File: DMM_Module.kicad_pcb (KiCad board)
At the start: 4 copper layers, 60 x 96 mm, 110 parts, among them J1 M20-7810245, J2 M20-7810245, J3 M20-7812045, J4 M20-7812045, J5 M20-7810245, J6 M20-7810245, K1 G6K-2F-Y-TR, K2 G6K-2F-Y-TR, K3 G6K-2F-Y-TR, K4 G6K-2F-Y-TR, Q1 DMN2056U, Q2 DMN2056U, Q3 DMN2056U, Q4 DMN2056U, U1 HY3131, U2 TPS7A2401DBVR, U3 PI4IOE5V9536UEX, U4 ADUM5411BRSZ, U5 NCP164CSN330T1G, X1 4.9152MHz

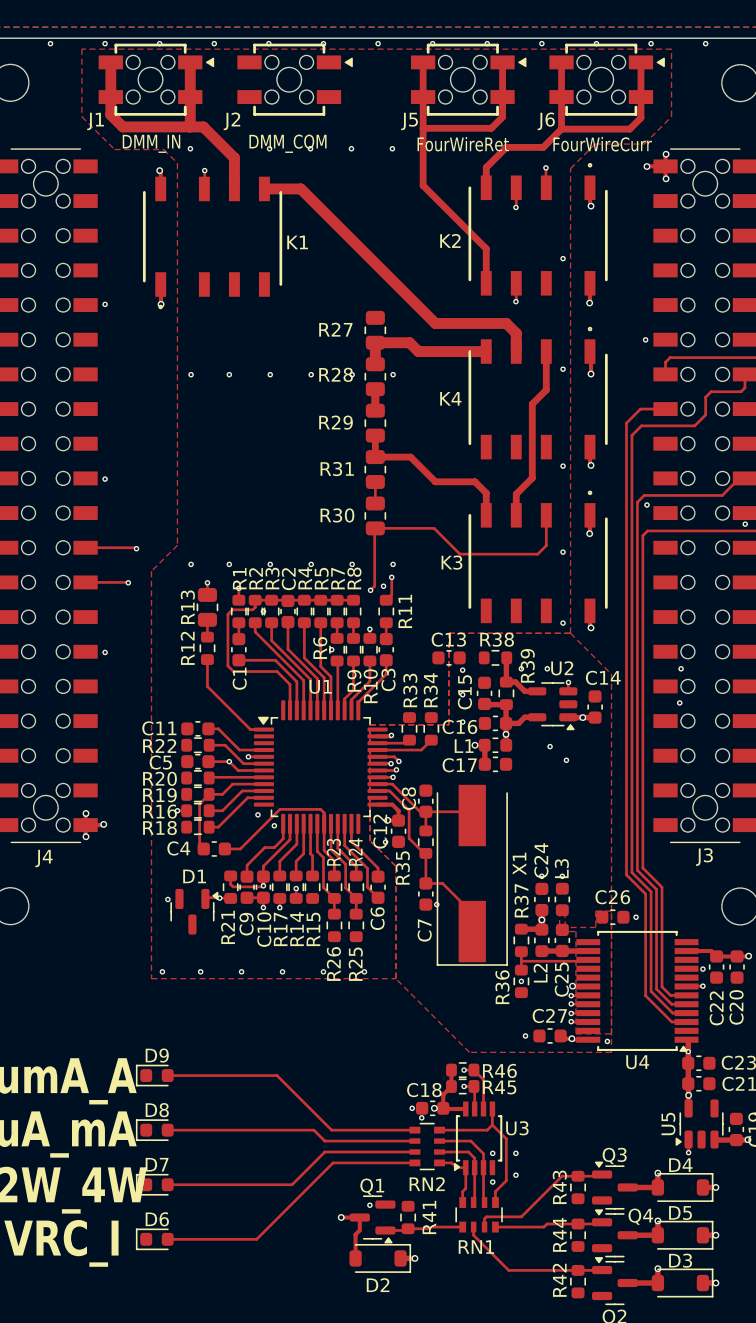
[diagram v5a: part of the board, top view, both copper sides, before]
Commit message: Schematics updated with current protection and EEPROM
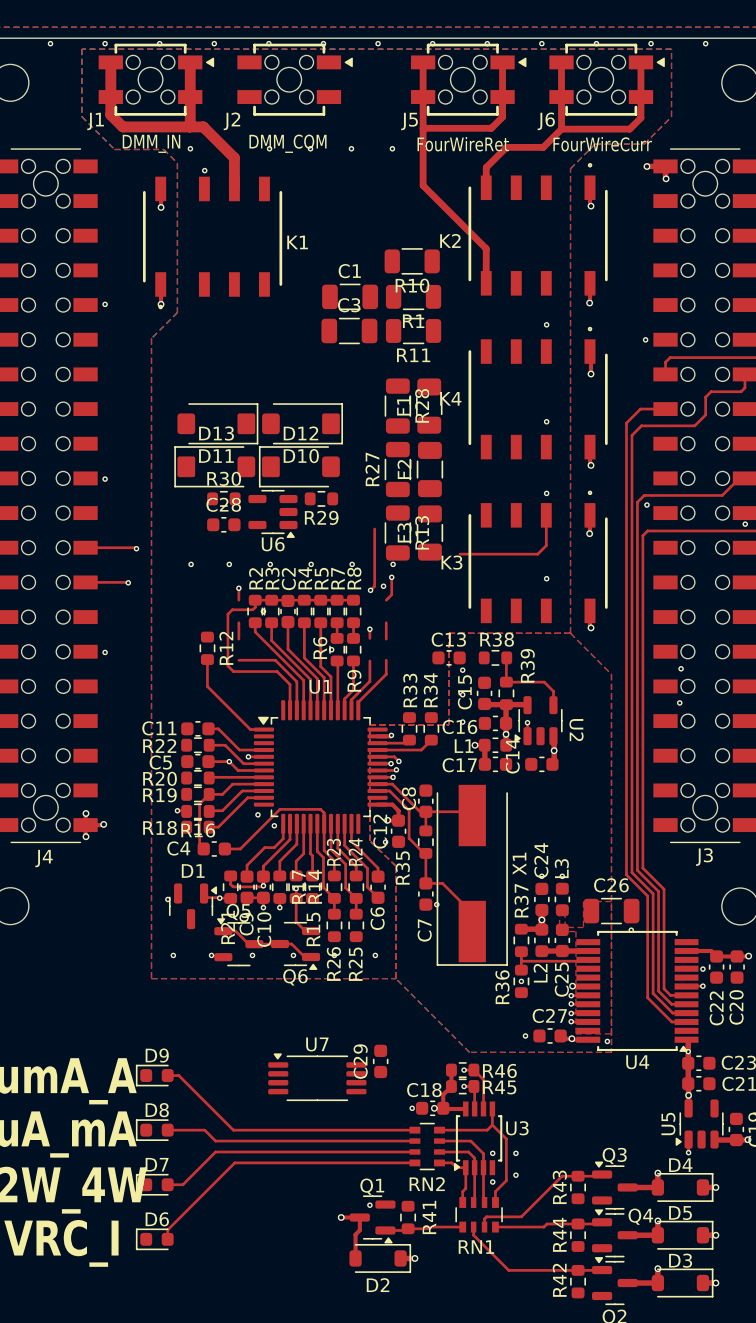
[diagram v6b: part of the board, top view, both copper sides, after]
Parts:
- removed R31: 75, Resistor_SMD:R_0805_2012Metric
- added C28: 100n, Capacitor_SMD:C_0603_1608Metric, F.Cu at (156.2, 71.2)
- added C29: 100n, Capacitor_SMD:C_0603_1608Metric, F.Cu at (167.7, 110.6)
- added D10: VS-3EJH01-M3, sesa_device:SlimSMPA, F.Cu at (161.8, 63.8)
- added D11: VS-3EJH01-M3, sesa_device:SlimSMPA, F.Cu at (155.6, 63.8)
- added D12: VS-3EJH01-M3, sesa_device:SlimSMPA, F.Cu at (161.8, 67.0)
- added D13: VS-3EJH01-M3, sesa_device:SlimSMPA, F.Cu at (155.6, 67.0)
- added F1: 50mA, Fuse:Fuse_1206_3216Metric, F.Cu at (171.2, 62.5)
- added F2: 500mA, Fuse:Fuse_1206_3216Metric, F.Cu at (171.3, 67.2)
- added F3: 2A, Fuse:Fuse_1206_3216Metric, F.Cu at (171.3, 71.8)
- added Q5: MMBT3904, Package_TO_SOT_SMD:SOT-23-3, F.Cu at (157.3, 102.0)
- added Q6: MMBT3904, Package_TO_SOT_SMD:SOT-23-3, F.Cu at (161.4, 102.0)
- added U6: TLV9061, Package_TO_SOT_SMD:SOT-23-5, F.Cu at (159.8, 70.3)
- added U7: AT24C08C, Package_SO:TSSOP-8_4.4x3mm_P0.65mm, F.Cu at (163.0, 111.8)
- C1, C3: value 5p1 -> 5p6; footprint Capacitor_SMD:C_0603_1608Metric -> Capacitor_SMD:C_1206_3216Metric
- C26: footprint Capacitor_SMD:C_0603_1608Metric -> Capacitor_SMD:C_1206_3216Metric
- R1, R10, R11: footprint Resistor_SMD:R_0603_1608Metric -> Resistor_SMD:R_1206_3216Metric
- R12: value 100 -> 10k
- R13: value 1k5 -> 20m; footprint Resistor_SMD:R_0805_2012Metric -> Resistor_SMD:R_1206_3216Metric
- R27: value 10m -> 1; footprint Resistor_SMD:R_0805_2012Metric -> Resistor_SMD:R_1206_3216Metric
- R28: value 910m -> 100; footprint Resistor_SMD:R_0805_2012Metric -> Resistor_SMD:R_1206_3216Metric
- R29: value 80m -> 10k; footprint Resistor_SMD:R_0805_2012Metric -> Resistor_SMD:R_0603_1608Metric
- R30: value 24 -> 100; footprint Resistor_SMD:R_0805_2012Metric -> Resistor_SMD:R_0603_1608Metric
- moved R10 28.6 mm to (170.0, 51.9), turned to 180 degrees
- moved C1 27.1 mm to (165.4, 54.5), turned to 0 degrees
- moved R1 26.4 mm to (170.1, 54.5), turned to 180 degrees
- moved C3 23.5 mm to (165.4, 57.0), turned to 0 degrees
- moved R11 20.6 mm to (170.1, 57.0), turned to 180 degrees
- moved R13 15.0 mm to (168.9, 71.8)
- moved R30 11.2 mm to (156.2, 69.3), turned to 0 degrees
- moved R27 10.3 mm to (168.9, 67.2)
- moved R29 6.81 mm to (163.3, 69.3), turned to 180 degrees
- moved C14 5.73 mm to (179.5, 88.8), turned to 0 degrees
- moved R28 2.71 mm to (168.9, 62.5)
- moved U2 1.50 mm to (179.4, 85.6), turned to 90 degrees
- moved C26 0.46 mm to (184.6, 99.5)
- moved D1 0.41 mm to (153.8, 99.2)
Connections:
- K1 pad 2: unconnected-(K1A-NC1-Pad2) -> /DMM DAQ/VdOhmCap
- K1 pad 3: unconnected-(K1A-COM1-Pad3) -> /DMM_IN
- K1 pad 4: unconnected-(K1A-NO1-Pad4) -> /DMM DAQ/CurrentIn
- K1 pad 5: /DMM DAQ/CurrentIn -> unconnected-(K1B-NO2-Pad5)
- K1 pad 6: /DMM_IN -> unconnected-(K1B-COM2-Pad6)
- K1 pad 7: /DMM DAQ/VdOhmCap -> unconnected-(K1B-NC2-Pad7)
- K2 pad 2: /DMM DAQ/VdOhmCap -> GNDA
- K2 pad 4: /FourWireCurr -> /FourWireRet
- K2 pad 5: /FourWireRet -> /FourWireCurr
- K2 pad 7: GNDA -> /DMM DAQ/mVOhmCap
- K3 pad 2: /DMM DAQ/I_uAmp -> Net-(K3A-NC1)
- K3 pad 4: /DMM DAQ/I_mAmp -> Net-(K3A-NO1)
- K4 pad 2: Net-(K3A-COM1) -> unconnected-(K4A-NC1-Pad2)
- K4 pad 3: /DMM DAQ/CurrentIn -> /DMM DAQ/mVOhmCap
- K4 pad 4: /DMM DAQ/I_Amp -> /DMM DAQ/VdOhmCap
- K4 pad 5: unconnected-(K4B-NO2-Pad5) -> Net-(K3A-COM1)
- K4 pad 6: unconnected-(K4B-COM2-Pad6) -> /DMM DAQ/CurrentIn
- K4 pad 7: unconnected-(K4B-NC2-Pad7) -> Net-(K4B-NC2)
- R12 pad 1: Net-(R12-Pad1) -> Net-(K2B-COM2)
- R13 pad 1: Net-(K2A-COM1) -> /DMM DAQ/I_Amp
- R13 pad 2: Net-(R12-Pad1) -> GNDA
- R14 pad 2: /DMM DAQ/VdOhmCap -> /DMM DAQ/mVOhmCap
- R16 pad 2: Net-(K2B-COM2) -> Net-(K2A-COM1)
- R27 pad 2: GNDA -> /DMM DAQ/I_mAmp
- R28 pad 1: /DMM DAQ/I_Amp -> /DMM DAQ/I_uAmp
- R28 pad 2: Net-(R28-Pad2) -> /DMM DAQ/I_mAmp
- R29 pad 1: /DMM DAQ/I_mAmp -> /DMM DAQ/I_uAmp
- R29 pad 2: Net-(R28-Pad2) -> Net-(U6-IN+)
- R30 pad 1: /DMM DAQ/I_uAmp -> Net-(D10-A)
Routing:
- net /DMM DAQ/VdOhmCap: track 104.5 -> 0.00 mm, vias 6 -> 0
- net /DMM DAQ/mVOhmCap: track 0.00 -> 58.2 mm, vias 0 -> 4
- net Net-(K2B-COM2): track 51.2 -> 0.00 mm, vias 2 -> 0
- net Net-(K2A-COM1): track 40.8 -> 0.68 mm, vias 2 -> 1
- net /DMM DAQ/CurrentIn: track 24.2 -> 0.00 mm
- net /DMM DAQ/I_uAmp: track 47.1 -> 31.3 mm
- net Net-(K3A-COM1): track 12.9 -> 0.00 mm
- net /DMM DAQ/I_mAmp: track 12.4 -> 0.00 mm
- net /DMM DAQ/I_Amp: track 9.97 -> 0.00 mm
- net Net-(K3A-NC1): track 0.00 -> 8.80 mm
- net Net-(Q5-D): track 0.00 -> 7.10 mm
- net GNDA: track 0.00 -> 2.79 mm, vias 34 -> 27
- net Net-(U2-FB): track 4.33 -> 6.53 mm
- net /5V_ISO: track 24.7 -> 22.6 mm
- net /Power/RELAY0: track 98.9 -> 96.7 mm
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- added copper zone on B.Cu, net GNDA
- added copper zone on B.Cu, net VSSA

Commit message: Isolated analog path is fully routed
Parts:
- added F4: 50mA, Fuse:Fuse_1206_3216Metric, F.Cu at (178.4, 55.2)
- D8: value uA_mA -> mA_uA
- D9: value umA_A -> A_umA
- moved Q5 56.7 mm to (167.3, 46.1)
- moved Q6 56.7 mm to (171.5, 46.1)
- moved R12 15.9 mm to (170.4, 76.3), turned to 180 degrees
- moved F1 9.31 mm to (171.6, 71.8), turned to -90 degrees
- moved F3 9.30 mm to (171.6, 62.5), turned to -90 degrees
- moved R13 9.30 mm to (169.0, 62.5), turned to 90 degrees
- moved R28 9.30 mm to (169.0, 71.8), turned to 90 degrees
- moved R10 5.93 mm to (164.2, 50.7), turned to -90 degrees
- moved C29 5.13 mm to (164.5, 106.5), turned to 0 degrees
- moved R29 4.01 mm to (162.6, 73.3)
- moved R30 3.25 mm to (159.4, 69.3)
- moved U7 2.85 mm to (162.1, 109.1)
- moved R45 2.50 mm to (171.2, 112.3)
- moved R46 2.50 mm to (171.2, 111.1)
- moved U6 1.87 mm to (159.4, 72.1), turned to 90 degrees
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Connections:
- K1 pad 6: unconnected-(K1B-COM2-Pad6) -> /DMM_IN
- K2 pad 7: /DMM DAQ/mVOhmCap -> Net-(K2B-NC2)
- Q6 pad 2: /DMM DAQ/mVOhmCap -> Net-(K2B-NC2)
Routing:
- net Net-(K2A-COM1): track 0.68 -> 60.6 mm, vias 1 -> 2
- net Net-(U1A-PA8): track 4.17 -> 37.0 mm, vias 0 -> 2
- net /DMM DAQ/VdOhmCap: track 0.00 -> 28.8 mm, vias 0 -> 2
- net Net-(K2B-COM2): track 0.00 -> 28.5 mm, vias 0 -> 2
- net VDDA: track 31.4 -> 59.0 mm, vias 2 -> 3
- net Net-(U1A-PA0): track 6.99 -> 33.7 mm, vias 0 -> 2
- net /DMM DAQ/CurrentIn: track 0.00 -> 25.7 mm
- net Net-(U1A-PA9): track 4.51 -> 29.9 mm, vias 0 -> 2
- net 3V3: track 36.1 -> 57.0 mm, vias 4 -> 5
- net /DMM DAQ/I_uAmp: track 31.3 -> 49.2 mm
- net Net-(K2B-NC2): track 0.00 -> 17.4 mm, vias 0 -> 2
- net VSSA: track 4.25 -> 20.6 mm, vias 12 -> 15
- net Net-(K4B-NC2): track 0.00 -> 13.8 mm
- net Net-(U6-IN-): track 0.00 -> 10.9 mm
- net /FourWireRet: track 28.3 -> 17.7 mm
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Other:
- board text added: "A_muA"
- board text added: "V_uV"
- board text added: "mA_uA"
- board text removed: "uA_mA"
- board text removed: "umA_A"
